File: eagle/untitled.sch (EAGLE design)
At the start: 34 parts, among them K1 AZ8-FORM-A, Q1 IRFZ24NPBF, U1 ATTINY85-20S, X1 MKDSN1,5/3-5,08, X2 MKDSN1,5/3-5,08

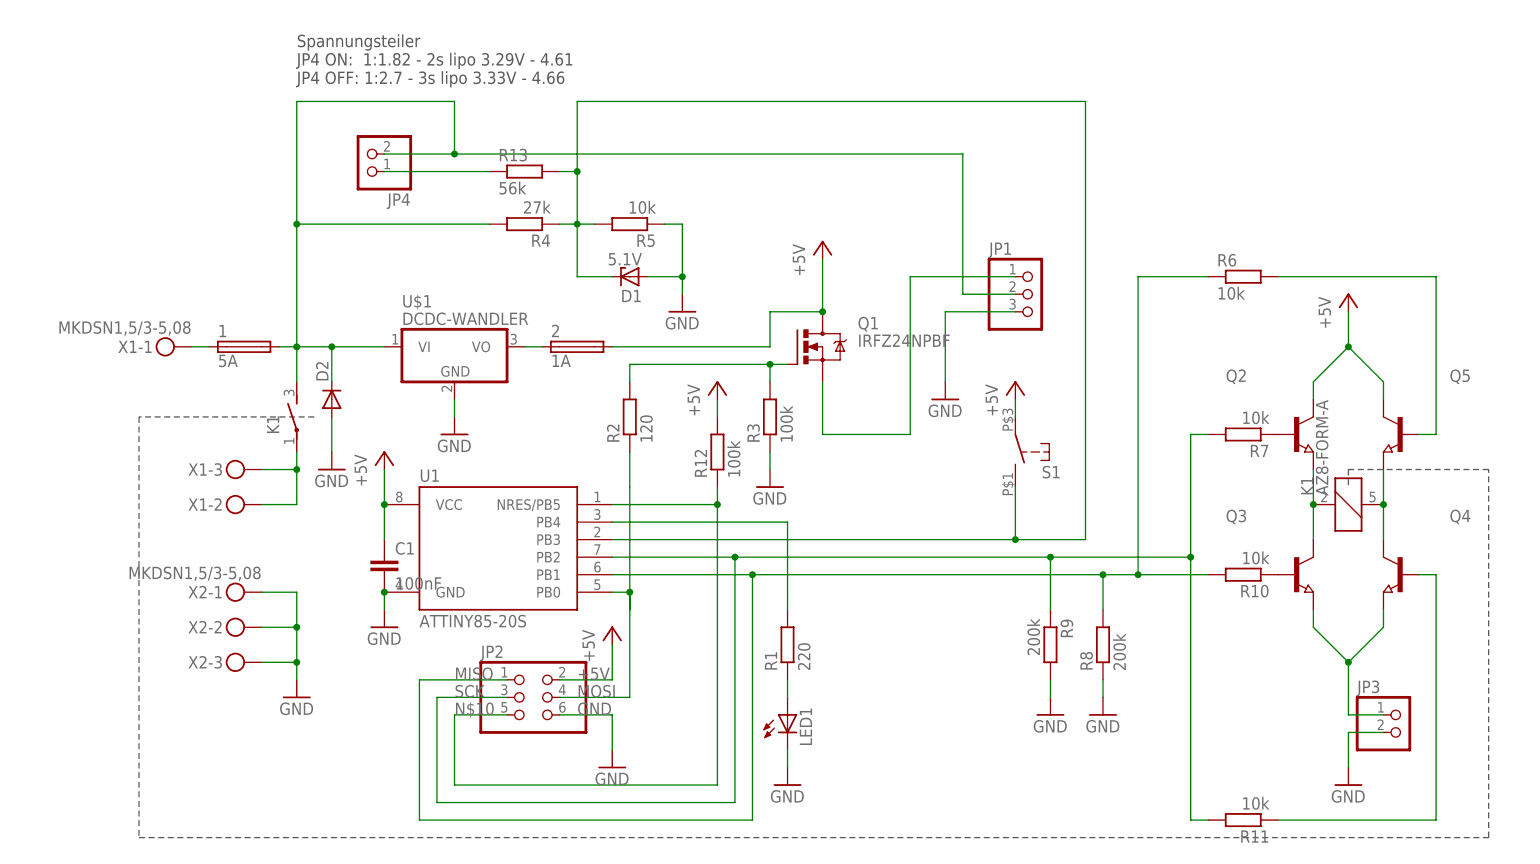
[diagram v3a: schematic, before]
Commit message: Changed relais. Fixed compiler failures
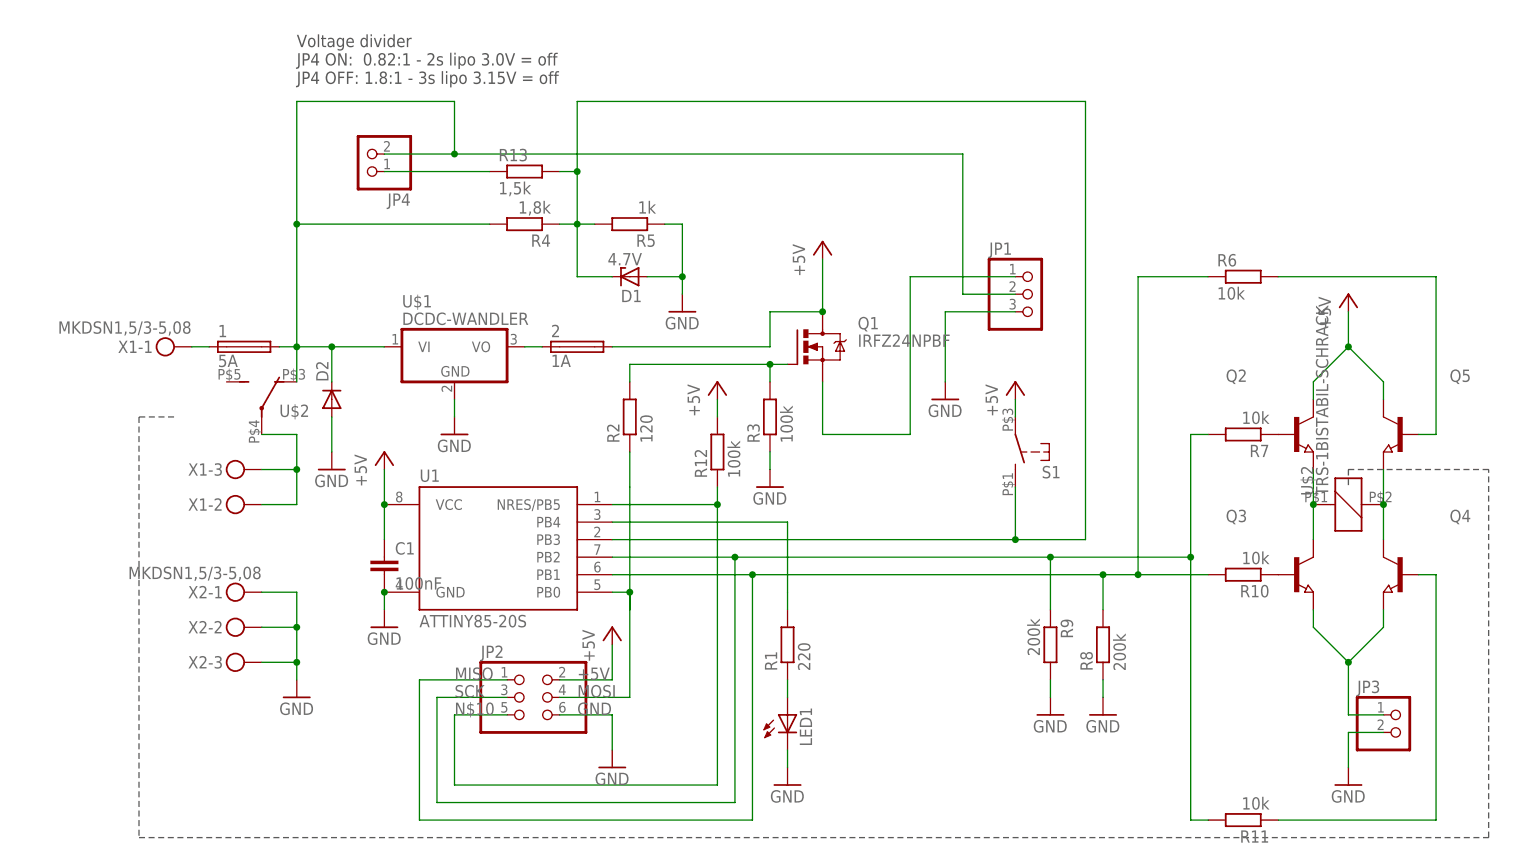
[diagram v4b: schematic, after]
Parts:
- removed K1: AZ8-FORM-A, 0liver:AZ8-FORM-A
- added U$2: TRS-1BISTABIL-SCHRACK, 0liver:TRS-1BISTABIL-SCHRACK
- D1: value 5.1V -> 4.7V
- R13: value 56k -> 1,5k
- R4: value 27k -> 1,8k
- R5: value 10k -> 1k
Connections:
- removed net N$3: K1-1.P, X1-2.KL, X1-3.KL
- new net N$17: U$2G$2.P, X1-2.KL, X1-3.KL
- net N$11: now also U$2G$1.1; no longer K1K.1
- net N$13: now also U$2G$1.2; no longer K1K.2
- net N$2: now also U$2G$2.O; no longer K1-1.S
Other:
- note added: "Voltage divider JP4 ON: 0.82:1 - 2s lipo 3.0V = off JP4 OFF: 1.8:1 - 3s lipo 3.15V = off"
- note removed: "Spannungsteiler JP4 ON: 1:1.82 - 2s lipo 3.29V - 4.61 JP4 OFF: 1:2.7 - 3s lipo 3.33V - 4.66"

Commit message: Updated info text in diagram
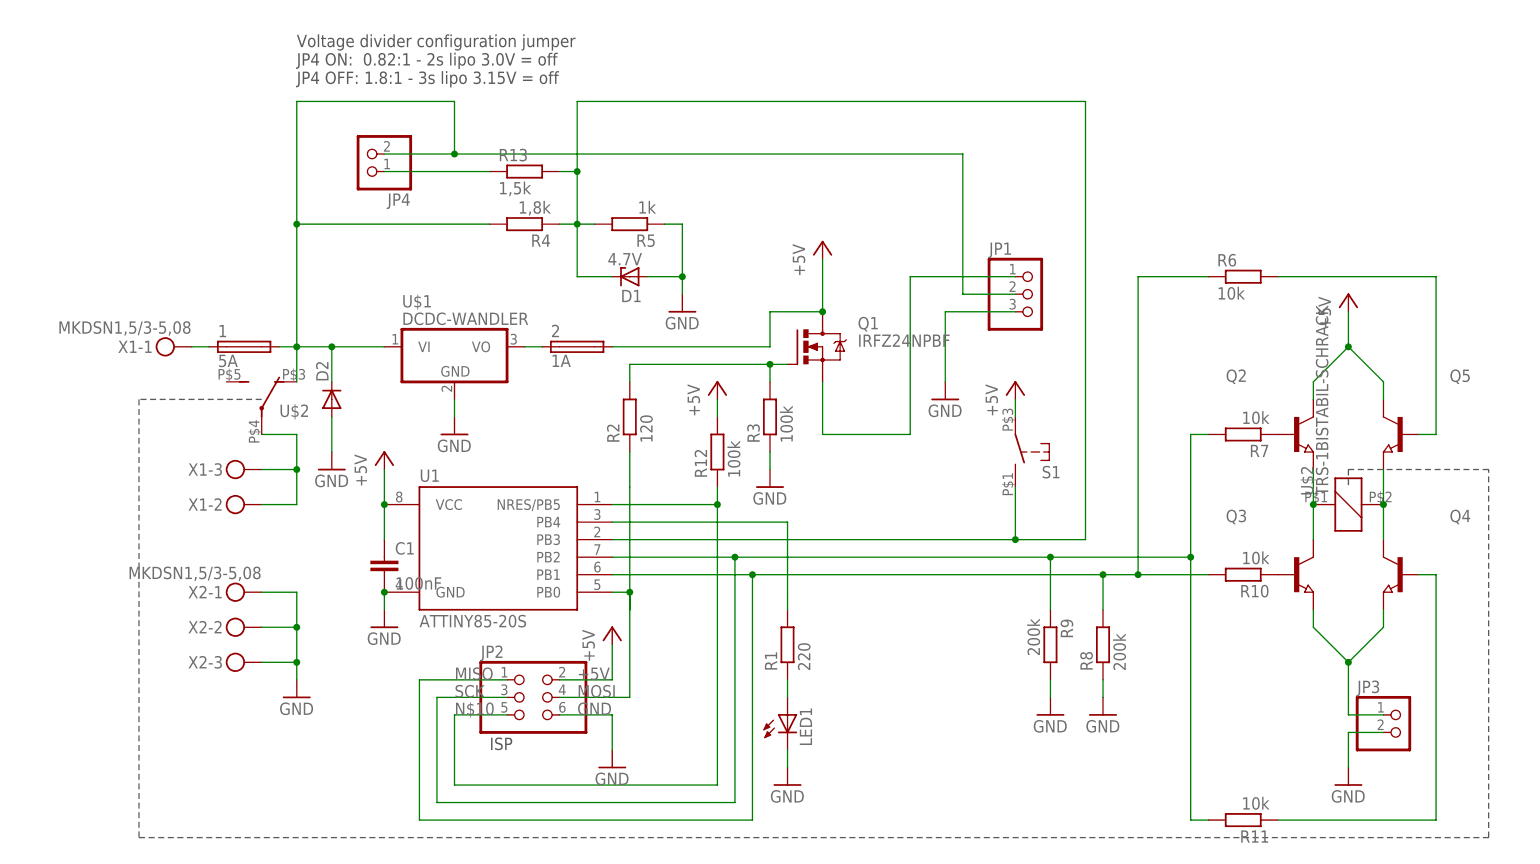
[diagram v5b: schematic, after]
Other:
- note added: "ISP"
- note added: "Voltage divider configuration jumper JP4 ON: 0.82:1 - 2s lipo 3.0V = off JP4 OFF: 1.8:1 - 3s lipo 3.15V = off"
- note removed: "Voltage divider JP4 ON: 0.82:1 - 2s lipo 3.0V = off JP4 OFF: 1.8:1 - 3s lipo 3.15V = off"
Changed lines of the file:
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@@
 <grid distance="0.1" unitdist="inch" unit="inch" style="lines" multiple="1" display="no" altdistance="0.01" altunitdist="inch" altunit="inch"/>
 <layers>
-<layer number="1" name="Top" color="4" fill="1" visible="yes" active="no"/>
-<layer number="16" name="Bottom" color="1" fill="1" visible="yes" active="no"/>
-<layer number="17" name="Pads" color="2" fill="1" visible="yes" active="no"/>
-<layer number="18" name="Vias" color="2" fill="1" visible="yes" active="no"/>
-<layer number="19" name="Unrouted" color="6" fill="1" visible="yes" active="no"/>
-<layer number="20" name="Dimension" color="15" fill="1" visible="yes" active="no"/>
-<layer number="21" name="tPlace" color="7" fill="1" visible="yes" active="no"/>
-<layer number="22" name="bPlace" color="7" fill="1" visible="yes" active="no"/>
-<layer number="23" name="tOrigins" color="15" fill="1" visible="yes" active="no"/>
-<layer number="24" name="bOrigins" color="15" fill="1" visible="yes" active="no"/>
-<layer number="25" name="tNames" color="7" fill="1" visible="yes" active="no"/>
-<layer number="26" name="bNames" color="7" fill="1" visible="yes" active="no"/>
-<layer number="27" name="tValues" color="7" fill="1" visible="yes" active="no"/>
-<layer number="28" name="bValues" color="7" fill="1" visible="yes" active="no"/>
+<layer number="1" name="Top" color="4" fill="1" visible="no" active="no"/>
+<layer number="16" name="Bottom" color="1" fill="1" visible="no" active="no"/>
+<layer number="17" name="Pads" color="2" fill="1" visible="no" active="no"/>
+<layer number="18" name="Vias" color="2" fill="1" visible="no" active="no"/>
+<layer number="19" name="Unrouted" color="6" fill="1" visible="no" active="no"/>
+<layer number="20" name="Dimension" color="15" fill="1" visible="no" active="no"/>
+<layer number="21" name="tPlace" color="7" fill="1" visible="no" active="no"/>
+<layer number="22" name="bPlace" color="7" fill="1" visible="no" active="no"/>
+<layer number="23" name="tOrigins" color="15" fill="1" visible="no" active="no"/>
+<layer number="24" name="bOrigins" color="15" fill="1" visible="no" active="no"/>
+<layer number="25" name="tNames" color="7" fill="1" visible="no" active="no"/>
+<layer number="26" name="bNames" color="7" fill="1" visible="no" active="no"/>
+<layer number="27" name="tValues" color="7" fill="1" visible="no" active="no"/>
+<layer number="28" name="bValues" color="7" fill="1" visible="no" active="no"/>
 <layer number="29" name="tStop" color="7" fill="3" visible="no" active="no"/>
 <layer number="30" name="bStop" color="7" fill="6" visible="no" active="no"/>
@@
 <layer number="35" name="tGlue" color="7" fill="4" visible="no" active="no"/>
 <layer number="36" name="bGlue" color="7" fill="5" visible="no" active="no"/>
-<layer number="37" name="tTest" color="7" fill="1" visible="yes" active="no"/>
-<layer number="38" name="bTest" color="7" fill="1" visible="yes" active="no"/>
+<layer number="37" name="tTest" color="7" fill="1" visible="no" active="no"/>
+<layer number="38" name="bTest" color="7" fill="1" visible="no" active="no"/>
 <layer number="39" name="tKeepout" color="4" fill="11" visible="no" active="no"/>
 <layer number="40" name="bKeepout" color="1" fill="11" visible="no" active="no"/>
@@
 <layer number="44" name="Drills" color="7" fill="1" visible="no" active="no"/>
 <layer number="45" name="Holes" color="7" fill="1" visible="no" active="no"/>
-<layer number="46" name="Milling" color="3" fill="1" visible="yes" active="no"/>
-<layer number="47" name="Measures" color="7" fill="1" visible="yes" active="no"/>
-<layer number="48" name="Document" color="7" fill="1" visible="yes" active="no"/>
-<layer number="49" name="Reference" color="7" fill="1" visible="yes" active="no"/>
-<layer number="51" name="tDocu" color="7" fill="1" visible="yes" active="no"/>
-<layer number="52" name="bDocu" color="7" fill="1" visible="yes" active="no"/>
+<layer number="46" name="Milling" color="3" fill="1" visible="no" active="no"/>
+<layer number="47" name="Measures" color="7" fill="1" visible="no" active="no"/>
+<layer number="48" name="Document" color="7" fill="1" visible="no" active="no"/>
+<layer number="49" name="Reference" color="7" fill="1" visible="no" active="no"/>
+<layer number="51" name="tDocu" color="7" fill="1" visible="no" active="no"/>
+<layer number="52" name="bDocu" color="7" fill="1" visible="no" active="no"/>
 <layer number="90" name="Modules" color="5" fill="1" visible="yes" active="yes"/>
 <layer number="91" name="Nets" color="2" fill="1" visible="yes" active="yes"/>
@@
 <sheet>
 <plain>
-<wire x1="-20.32" y1="78.74" x2="-25.4" y2="78.74" width="0.1524" layer="97" style="shortdash"/>
-<wire x1="-25.4" y1="78.74" x2="-25.4" y2="17.78" width="0.1524" layer="97" style="shortdash"/>
+<wire x1="-7.62" y1="81.28" x2="-25.4" y2="81.28" width="0.1524" layer="97" style="shortdash"/>
+<wire x1="-25.4" y1="81.28" x2="-25.4" y2="17.78" width="0.1524" layer="97" style="shortdash"/>
 <wire x1="-25.4" y1="17.78" x2="170.18" y2="17.78" width="0.1524" layer="97" style="shortdash"/>
 <wire x1="170.18" y1="17.78" x2="170.18" y2="71.12" width="0.1524" layer="97" style="shortdash"/>
 <wire x1="170.18" y1="71.12" x2="149.86" y2="71.12" width="0.1524" layer="97" style="shortdash"/>
 <wire x1="149.86" y1="71.12" x2="149.86" y2="68.58" width="0.1524" layer="97" style="shortdash"/>
-<text x="-2.54" y="127" size="1.778" layer="97">Voltage divider
+<text x="-2.54" y="127" size="1.778" layer="97">Voltage divider configuration jumper
 JP4 ON:  0.82:1 - 2s lipo 3.0V = off
 JP4 OFF: 1.8:1 - 3s lipo 3.15V = off</text>
+<text x="25.4" y="30.48" size="1.778" layer="97">ISP</text>
 </plain>
 <instances>

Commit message: Lots of essential changes to functionality
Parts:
- R10, R11, R6, R7: value 10k -> 6,8k
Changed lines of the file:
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@@
 <part name="P+4" library="supply1" deviceset="+5V" device=""/>
 <part name="P+5" library="supply1" deviceset="+5V" device=""/>
-<part name="R6" library="rcl" deviceset="R-EU_" device="R1206" value="10k"/>
-<part name="R7" library="rcl" deviceset="R-EU_" device="R1206" value="10k"/>
-<part name="R10" library="rcl" deviceset="R-EU_" device="R1206" value="10k"/>
-<part name="R11" library="rcl" deviceset="R-EU_" device="R1206" value="10k"/>
+<part name="R6" library="rcl" deviceset="R-EU_" device="R1206" value="6,8k"/>
+<part name="R7" library="rcl" deviceset="R-EU_" device="R1206" value="6,8k"/>
+<part name="R10" library="rcl" deviceset="R-EU_" device="R1206" value="6,8k"/>
+<part name="R11" library="rcl" deviceset="R-EU_" device="R1206" value="6,8k"/>
 <part name="P+6" library="supply1" deviceset="+5V" device=""/>
 <part name="R12" library="rcl" deviceset="R-EU_" device="R1206" value="100k"/>

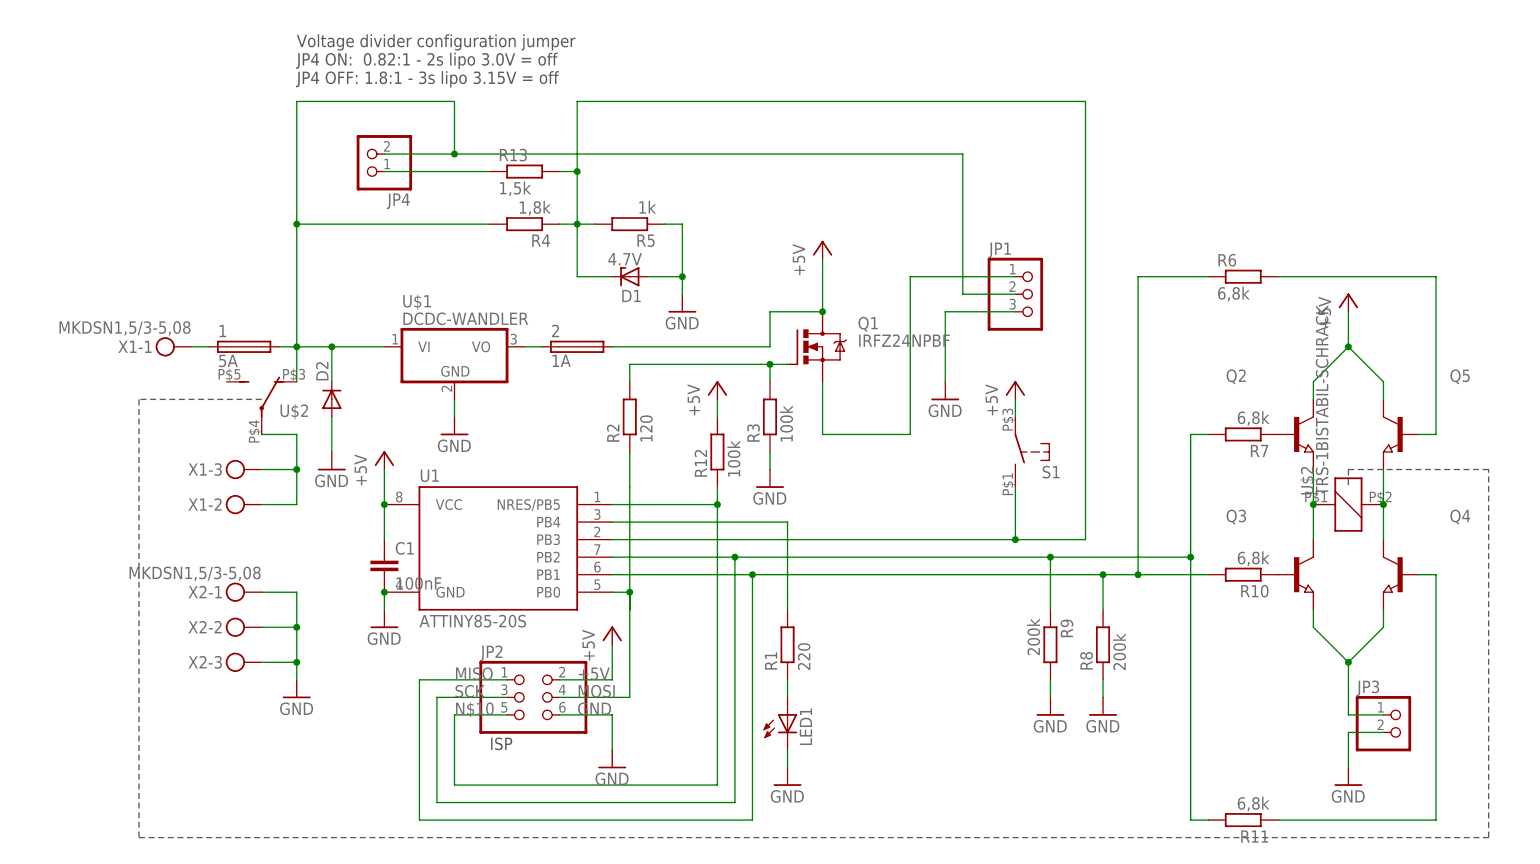
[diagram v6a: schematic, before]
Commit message: Updated to version 2.1 with mosfets instead of a relay
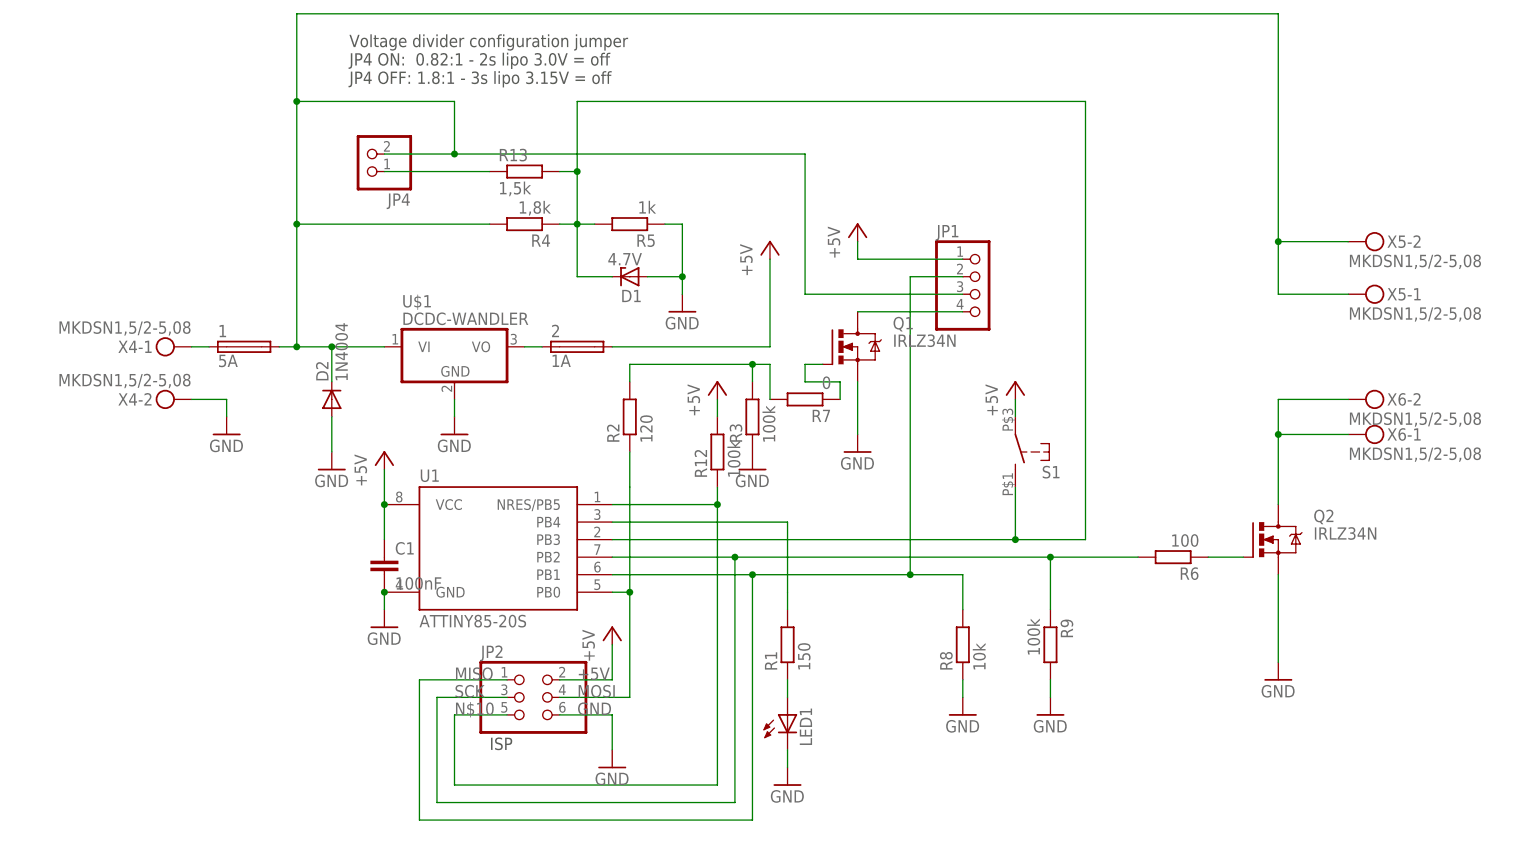
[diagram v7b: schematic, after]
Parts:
- removed JP3: (no value), pinhead:PINHD-1X2
- removed Q3, Q4, Q5: (no value), semicon-smd-ipc:NPN-TRANSISTOR_SOT23
- removed R10, R11: 6,8k, rcl:R-EU_R1206
- removed U$2: TRS-1BISTABIL-SCHRACK, 0liver:TRS-1BISTABIL-SCHRACK
- removed X1, X2: MKDSN1,5/3-5,08, con-phoenix-508:MKDSN1,5/3-5,08
- added X4, X5, X6: MKDSN1,5/2-5,08, con-phoenix-508:MKDSN1,5/2-5,08
- D2: value (none) -> 1N4004; device diode:DIODE-DO201-15 -> diode:1N4004
- JP1: device pinhead:PINHD-1X3 -> pinhead:PINHD-1X4
- Q1: value IRFZ24NPBF -> IRLZ34N
- Q2: value (none) -> IRLZ34N; device semicon-smd-ipc:NPN-TRANSISTOR_SOT23 -> 0liver:IRLZ44Z
- R1: value 220 -> 150
- R6: value 6,8k -> 100
- R7: value 6,8k -> 0
- R8: value 200k -> 10k
- R9: value 200k -> 100k
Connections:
- removed net N$11: Q2.E, Q3.C, U$2G$1.1
- removed net N$13: Q4.C, Q5.E, U$2G$1.2
- removed net N$14: Q5.B, R6.2
- removed net N$15: Q2.B, R7.1
- removed net N$17: U$2G$2.P, X1-2.KL, X1-3.KL
- removed net N$19: Q3.B, R10.1
- removed net N$20: Q4.B, R11.1
- removed net N$9: JP1.1, Q1.S
- new net N$21: JP1.4, Q1.D
- new net N$3: Q2.D, X6-1.KL, X6-2.KL
- new net N$7: Q1.G, R7.1
- net +5V: now also JP1.1; no longer Q1.D, Q2.C, Q5.C
- net GND: now also Q1.S, Q2.S, X4-2.KL; no longer JP1.3, JP3.2, X2-1.KL, X2-2.KL, X2-3.KL
- net MISO: now also JP1.2; no longer R10.2, R6.1
- net N$1: now also X4-1.KL; no longer X1-1.KL
- net N$2: now also JP1.3, X5-1.KL, X5-2.KL; no longer JP1.2, U$2G$2.O
- net N$4: now also Q2.G, R6.1; no longer JP3.1, Q3.E, Q4.E
- net N$8: now also R7.2; no longer Q1.G
- net SCK: now also R6.2; no longer R11.2, R7.2
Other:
- moved on the sheet: Q1, R3, R6, R7, R8
